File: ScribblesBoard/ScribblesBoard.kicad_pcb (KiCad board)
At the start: 2 copper layers, 49.5 x 12.7 mm, 22 parts, among them J1 ICSP, J2 Conn_01x04, U1 MIC5205-3.3, U2 ATMEGA328P-MU, U3 BNO055

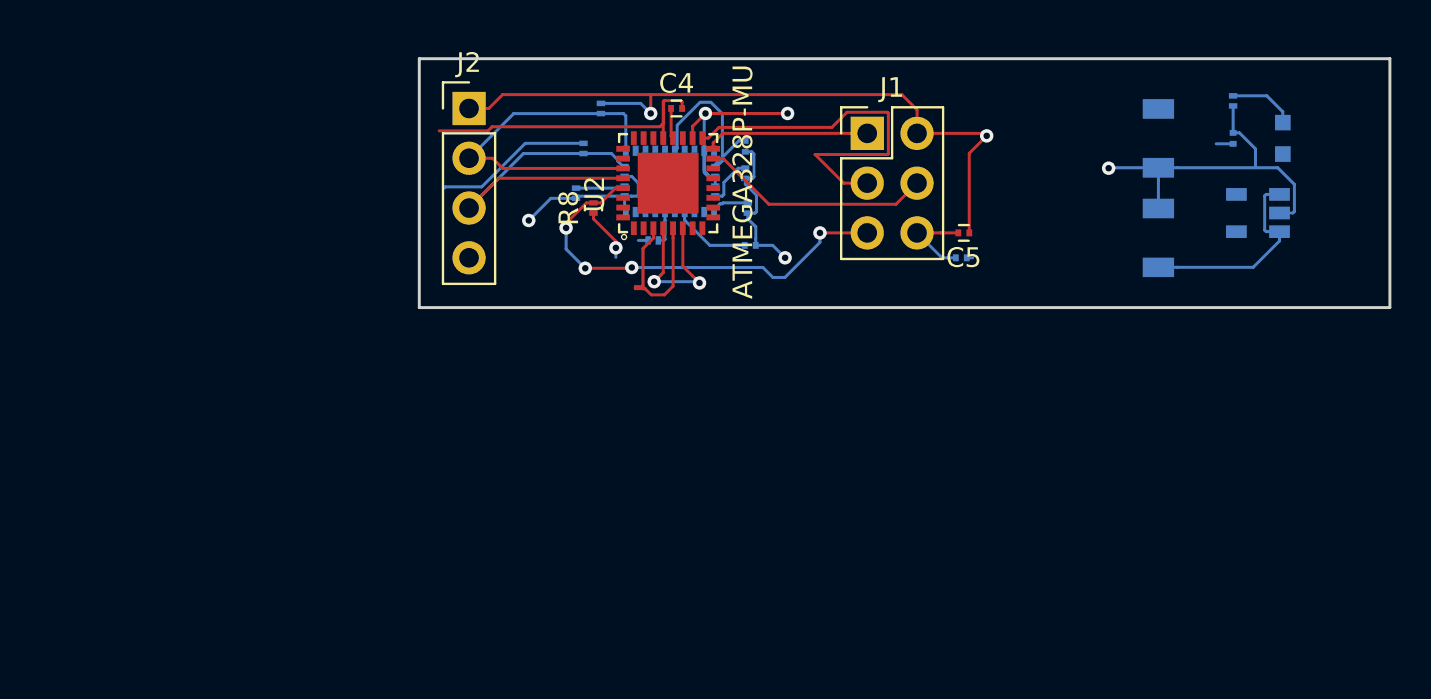
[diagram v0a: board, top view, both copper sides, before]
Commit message: Board without external oscillator
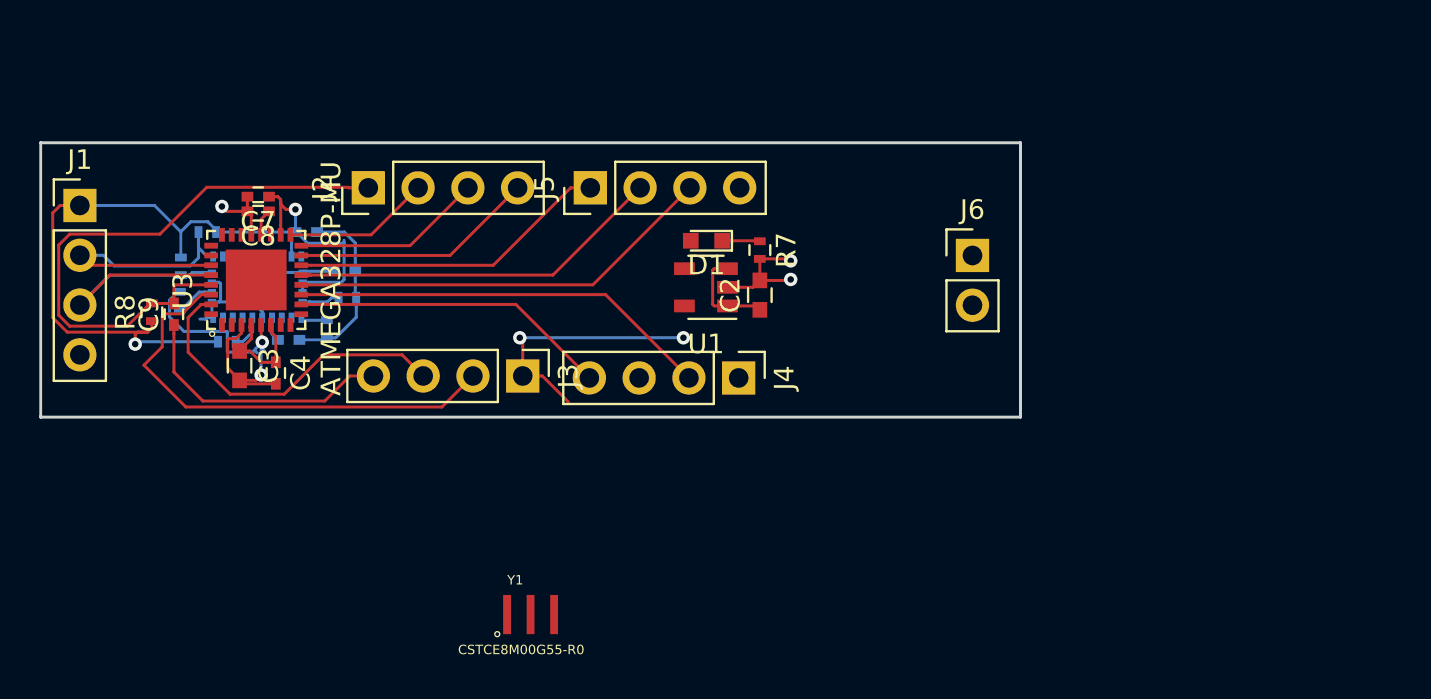
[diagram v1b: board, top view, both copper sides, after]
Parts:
- added C9: 0.1uF, Capacitors_SMD:C_0402, F.Cu at (134.8, 105.8)
- added J3: FTDI, Pin_Headers:Pin_Header_Straight_1x04_Pitch2.54mm, F.Cu at (152.6, 108.9)
- added J4: Bluetooth Connector 1, Pin_Headers:Pin_Header_Straight_1x04_Pitch2.54mm, F.Cu at (163.6, 109.0)
- added J5: Bluetooth Connector 2, Pin_Headers:Pin_Header_Straight_1x04_Pitch2.54mm, F.Cu at (156.1, 99.3)
- added J6: Battery Connection, Pin_Headers:Pin_Header_Straight_1x02_Pitch2.54mm, F.Cu at (175.6, 102.8)
- added Y1: CSTCE8M00G55-R0, CSTCE8M00G55-R0:OSC_CSTCE8M00G55-R0, F.Cu at (153.0, 121.1)
- C1: value 10uF -> 0.1uF; footprint Capacitors_SMD:C_1206 -> Capacitors_SMD:C_0402
- C2: footprint Capacitors_SMD:C_1206 -> Capacitors_SMD:C_0603; moved to F.Cu
- C3: value 0.1uF -> 10uF; footprint Capacitors_SMD:C_0201 -> Capacitors_SMD:C_0603; moved to F.Cu
- C4, C6: footprint Capacitors_SMD:C_0201 -> Capacitors_SMD:C_0402
- C5: footprint Capacitors_SMD:C_0201 -> Capacitors_SMD:C_0402; moved to B.Cu
- C7, C8: footprint Capacitors_SMD:C_0201 -> Capacitors_SMD:C_0402; moved to F.Cu
- D1, U1: moved to F.Cu
- J1: value ICSP -> Conn_01x04; footprint Pin_Headers:Pin_Header_Straight_2x03_Pitch2.54mm -> Pin_Headers:Pin_Header_Straight_1x04_Pitch2.54mm
- J2: value Conn_01x04 -> ICSP
- R1, R2, R3, R4, R5, R6: footprint Resistors_SMD:R_0201 -> Resistors_SMD:R_0402
- R7: footprint Resistors_SMD:R_0201 -> Resistors_SMD:R_0402; moved to F.Cu
- R8: value R_Small -> 10K; footprint Resistors_SMD:R_0201 -> Resistors_SMD:R_0402
- U2: value ATMEGA328P-MU -> BNO055; footprint VQFN-ATMEGA328P-MU:QFN50P500X500X100-33N -> BNO055:LGA28R50P4X10_380X520X100; moved to B.Cu
- U3: value BNO055 -> ATMEGA328P-MU; footprint BNO055:LGA28R50P4X10_380X520X100 -> VQFN-ATMEGA328P-MU:QFN50P500X500X100-33N; moved to F.Cu
- moved C3 52.0 mm to (138.2, 108.4), turned to 270 degrees
- moved R1 46.3 mm to (143.7, 104.9), turned to 180 degrees
- moved C1 44.7 mm to (140.7, 107.1), turned to 180 degrees
- moved J1 40.3 mm to (130.0, 100.2)
- moved C7 36.0 mm to (139.1, 99.8), turned to 180 degrees
- moved C5 33.6 mm to (141.6, 101.6)
- moved D1 29.9 mm to (162.0, 102.0), turned to 180 degrees
- moved R4 29.4 mm to (135.1, 105.1)
- moved R2 29.2 mm to (135.2, 103.3)
- moved U1 28.4 mm to (161.9, 104.4)
- moved C8 25.1 mm to (139.1, 100.5), turned to 180 degrees
- moved C4 24.5 mm to (140.0, 108.8), turned to 270 degrees
- moved R8 23.2 mm to (133.7, 105.7)
- moved R6 22.5 mm to (137.5, 107.2), turned to 0 degrees
- moved C2 21.9 mm to (164.7, 104.8), turned to 90 degrees
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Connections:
- C1 pad 1: /RAW -> GND
- C1 pad 2: GND -> Net-(C1-Pad2)
- C2 pad 1: /VCC -> /RAW
- C4 pad 1: Net-(C4-Pad1) -> /VCC
- C5 pad 1: /VCC -> GND
- C5 pad 2: GND -> /VCC
- C7 pad 1: GND -> /VCC
- C7 pad 2: /VCC -> GND
- C8 pad 1: GND -> Net-(C8-Pad1)
- C8 pad 2: Net-(C8-Pad2) -> GND
- J1 pad 1: /MISO -> /VCC
- J1 pad 2: /VCC -> /SDA_3V
- J1 pad 3: /SCK -> /SCL_3V
- J1 pad 4: /MOSI -> GND
- J2 pad 1: /VCC -> /RESET
- J2 pad 2: /SDA_3V -> /SCK
- J2 pad 3: /SCL_3V -> /MISO
- J2 pad 4: GND -> /MOSI
- R1 pad 1: Net-(D1-Pad1) -> GND
- R1 pad 2: GND -> /PS1_3V
- R2 pad 1: GND -> /SCL_3V
- R2 pad 2: /PS1_3V -> /VCC
- R3 pad 1: /SCL_3V -> GND
- R3 pad 2: /VCC -> /PS0_3V
- R4 pad 1: GND -> /I2CADDR_3V
- R4 pad 2: /PS0_3V -> GND
- R5 pad 1: /I2CADDR_3V -> /SDA_3V
- R5 pad 2: GND -> /VCC
- R6 pad 1: /SDA_3V -> /VCC
- R6 pad 2: /VCC -> Net-(R6-Pad2)
- R7 pad 1: /VCC -> Net-(D1-Pad1)
- R7 pad 2: Net-(R7-Pad2) -> GND
- U2 pad 1: Net-(U2-Pad1) -> (no net)
- U2 pad 10: Net-(U2-Pad10) -> GND
- U2 pad 11: Net-(U2-Pad11) -> Net-(R6-Pad2)
- U2 pad 12: Net-(U2-Pad12) -> (no net)
- U2 pad 13: Net-(U2-Pad13) -> (no net)
- U2 pad 15: /MOSI -> GND
- U2 pad 16: /MISO -> GND
- U2 pad 17: /SCK -> /I2CADDR_3V
- U2 pad 18: /VCC -> GND
- U2 pad 19: Net-(U2-Pad19) -> /SCL_3V
- U2 pad 2: Net-(U2-Pad2) -> Net-(C6-Pad2)
- U2 pad 20: Net-(C4-Pad1) -> /SDA_3V
- U2 pad 21: GND -> (no net)
- U2 pad 22: Net-(U2-Pad22) -> (no net)
- U2 pad 23: Net-(U2-Pad23) -> (no net)
- U2 pad 24: Net-(U2-Pad24) -> (no net)
- U2 pad 25: Net-(U2-Pad25) -> Net-(C6-Pad2)
- U2 pad 27: /SDA_3V -> Net-(U2-Pad27)
- U2 pad 28: /SCL_3V -> /VCC
- U2 pad 3: GND -> /VCC
- U2 pad 5: GND -> /PS1_3V
- U2 pad 6: /VCC -> /PS0_3V
- U2 pad 7: Net-(U2-Pad7) -> (no net)
- U2 pad 8: Net-(U2-Pad8) -> (no net)
- U2 pad 9: Net-(U2-Pad9) -> Net-(C1-Pad2)
- U3 pad 1: (no net) -> Net-(U3-Pad1)
- U3 pad 10: GND -> /D6
- U3 pad 11: Net-(R7-Pad2) -> /D7
- U3 pad 12: (no net) -> /D8
- U3 pad 13: (no net) -> /CTS_3V
- U3 pad 14: Net-(U3-Pad14) -> /D10
- U3 pad 15: GND -> /MOSI
- U3 pad 16: GND -> /MISO
- U3 pad 17: /I2CADDR_3V -> /SCK
- U3 pad 18: GND -> /VCC
- U3 pad 19: /SCL_3V -> Net-(U3-Pad19)
- U3 pad 2: Net-(C8-Pad2) -> Net-(U3-Pad2)
- U3 pad 20: /SDA_3V -> Net-(C8-Pad1)
- U3 pad 21: (no net) -> GND
- U3 pad 22: (no net) -> Net-(U3-Pad22)
- U3 pad 23: (no net) -> Net-(U3-Pad23)
- U3 pad 24: (no net) -> Net-(U3-Pad24)
- U3 pad 25: Net-(C8-Pad2) -> Net-(U3-Pad25)
- U3 pad 27: Net-(U3-Pad27) -> /SDA_3V
- U3 pad 28: /VCC -> /SCL_3V
- U3 pad 3: /VCC -> GND
- U3 pad 5: /PS1_3V -> GND
- U3 pad 6: /PS0_3V -> /VCC
- U3 pad 7: (no net) -> Net-(U3-Pad7)
- U3 pad 8: (no net) -> Net-(U3-Pad8)
- U3 pad 9: Net-(C6-Pad2) -> Net-(U3-Pad9)
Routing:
- net /RX_FTDI: track 0.00 -> 24.2 mm
- net GND: track 66.8 -> 42.9 mm, vias 3 -> 5
- net /D8: track 0.00 -> 21.9 mm
- net /D7: track 0.00 -> 21.5 mm
- net /CTS_3V: track 0.00 -> 19.6 mm
- net /TX_FTDI: track 0.00 -> 17.4 mm
- net /D10: track 0.00 -> 16.4 mm
- net /D6: track 0.00 -> 16.3 mm
- net /DTR: track 0.00 -> 13.7 mm
- net /SCK: track 19.1 -> 7.50 mm
- net Net-(C8-Pad2): track 9.43 -> 0.00 mm
- net /RESET: track 22.2 -> 30.0 mm, vias 4 -> 0
- net /VCC: track 69.8 -> 63.9 mm, vias 7 -> 4
- net /RAW: track 10.5 -> 5.06 mm
- net /SCL_3V: track 17.9 -> 14.8 mm
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- added copper zone on F.Cu, net /VCC
- added copper zone on B.Cu, net GND
- removed copper zone on B.Cu, net /VCC
- removed copper zone on F.Cu, net GND
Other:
- board size 49.5 x 12.7 mm -> 50 x 14 mm

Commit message: Added oscillator to imu
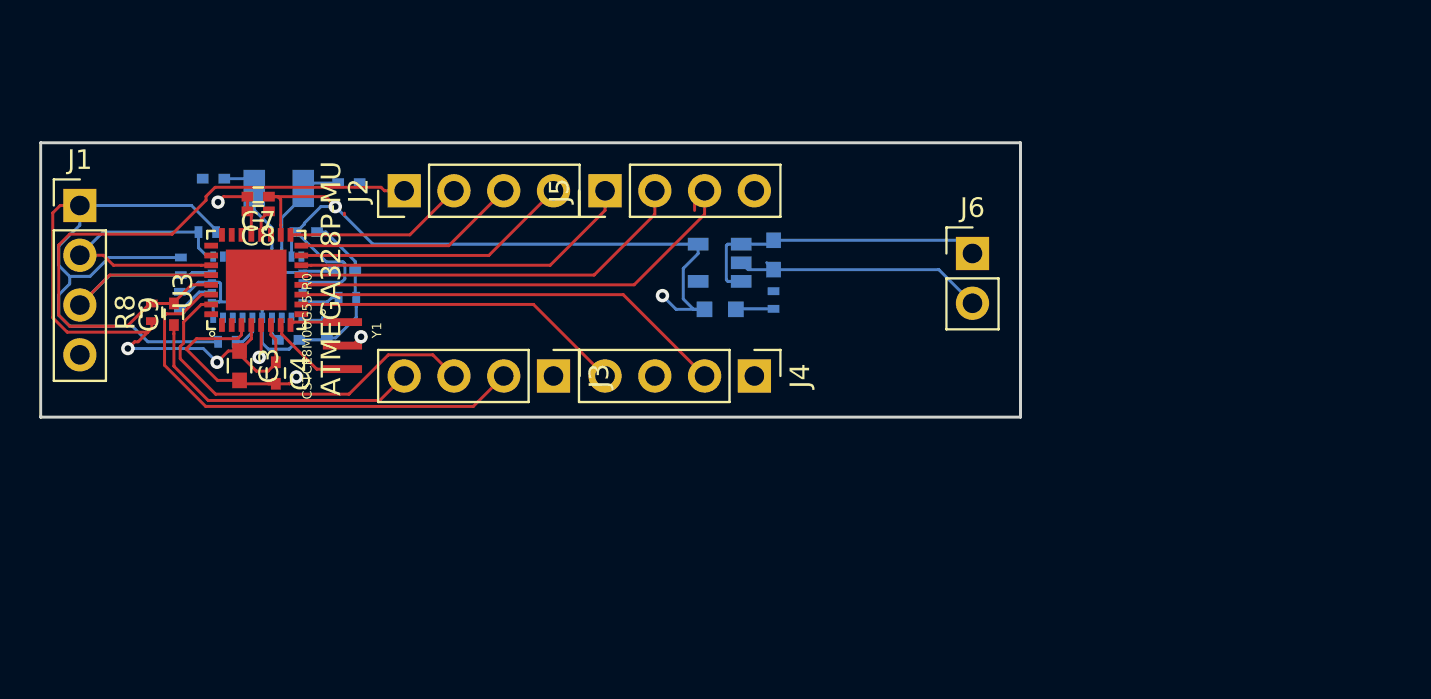
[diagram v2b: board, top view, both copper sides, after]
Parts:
- added C10: 22pF, Capacitors_SMD:C_0402, B.Cu at (143.7, 99.1)
- added C11: 22pF, Capacitors_SMD:C_0402, B.Cu at (136.8, 98.8)
- added Y2: Crystal, lib_fp:ECS-.327-12.5-34B-TR, B.Cu at (140.2, 99.3)
- C2, D1, R7, U1: moved to B.Cu
- moved Y1 16.7 mm to (143.4, 107.3), turned to 270 degrees
- moved D1 3.57 mm to (162.7, 105.5)
- moved R7 2.64 mm to (165.4, 105.0), turned to 90 degrees
- moved C2 2.17 mm to (165.4, 102.7), turned to 270 degrees
- moved J2 1.84 mm to (146.6, 99.5)
- moved J3 1.57 mm to (154.2, 108.9)
- moved U1 1.43 mm to (162.7, 103.1)
- moved J4 0.81 mm to (164.4, 108.9)
- moved J5 0.76 mm to (156.8, 99.5)
- moved J6 0.10 mm to (175.6, 102.7)
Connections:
- J3 pad 1: /VCC -> Net-(J3-Pad1)
- J6 pad 1: /3.3V -> /RAW
- U2 pad 26: Net-(U2-Pad26) -> /OSC2
- U2 pad 27: Net-(U2-Pad27) -> /OSC1
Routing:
- net /VCC: track 63.9 -> 98.2 mm
- net /RAW: track 5.06 -> 15.5 mm
- net GND: track 42.9 -> 49.7 mm, vias 5 -> 4
- net /OSC1: track 0.00 -> 5.82 mm
- net /OSC2: track 0.00 -> 5.59 mm
- net Net-(U3-Pad7): track 0.00 -> 4.32 mm
- net Net-(U3-Pad8): track 0.00 -> 2.71 mm
- net /D8: track 21.9 -> 24.3 mm
- net /TX_FTDI: track 17.4 -> 19.7 mm
- net /SCK: track 7.50 -> 9.27 mm
- net /MOSI: track 12.5 -> 14.2 mm
- net /MISO: track 9.72 -> 11.5 mm
- net /RESET: track 30.0 -> 31.5 mm
- net /DTR: track 13.7 -> 15.1 mm
- net /D10: track 16.4 -> 17.7 mm
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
